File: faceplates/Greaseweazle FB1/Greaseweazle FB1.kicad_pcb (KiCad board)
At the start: 2 copper layers, 90 x 94 mm, 6 parts, among them M1 Mounting, M2 Mounting, M3 Mounting, M4 Mounting

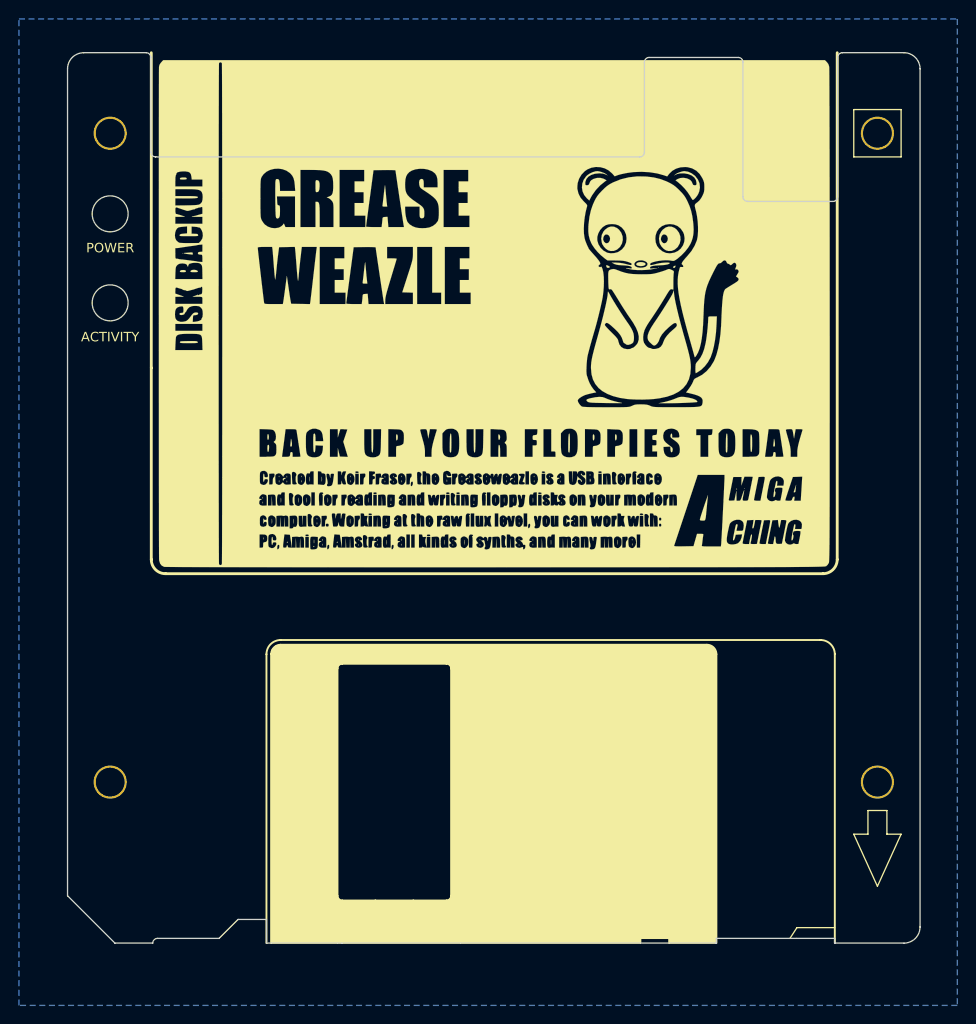
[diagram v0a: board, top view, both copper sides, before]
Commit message: Greaseweazle faceplate with amstrad cutout
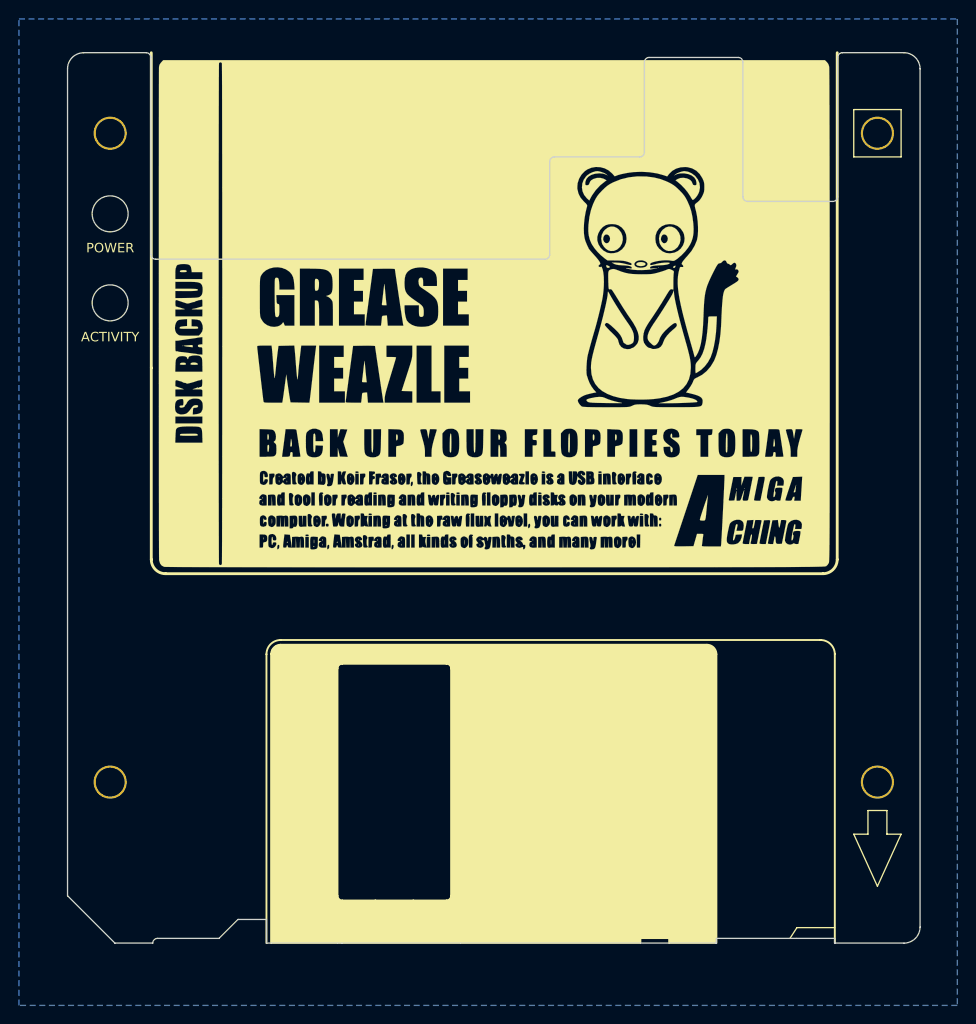
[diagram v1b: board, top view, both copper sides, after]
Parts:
- G***: footprint artwork:greaseweazle_label_cropped -> artwork:greaseweazle_label_amstrad
- moved REF** 27.7 mm to (180.0, 83.0)
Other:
- outline, holes or cut-outs redrawn
- board text added: "Amiga DrawBridge (Greaseweazle) github.com/tebl"
- board text removed: "Amiga DrawBridge (GreaseWeazle) github.com/tebl"
